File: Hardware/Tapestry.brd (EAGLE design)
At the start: 76.2 x 73.7 mm, 106 parts, among them J1 CORTEX_DEBUGPTH, J2 POWER_JACKPTH_LOCK, U1 ATSAMS70NXXA-AN, U2 AK4618VQSFE-PACKAGE, U3 LM1117, U4 LM1117, Y1 12MHz

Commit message: Routing in progress.
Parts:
- added J10: 3.3V, SparkFun-Passives:TP_15TH
- added J11: VIN, SparkFun-Passives:TP_15TH
- added J3: AOUT4L, SparkFun-Passives:TP_15TH
- added J4: AOUT4R, SparkFun-Passives:TP_15TH
- added J5: AOUT5L, SparkFun-Passives:TP_15TH
- added J6: AOUT5R, SparkFun-Passives:TP_15TH
- added J7: AIN3R, SparkFun-Passives:TP_15TH
- added J8: AIN3L, SparkFun-Passives:TP_15TH
- added J9: 3.3VA, SparkFun-Passives:TP_15TH
- TP2: device SparkFun-Connectors:1X06_NO_SILK -> SparkFun-Connectors:1X07_NO_SILK
- moved SJ2 6.60 mm to (54.9, 45.4)
- moved C34 5.08 mm to (44.5, 26.7)
- moved C3 4.58 mm to (36.8, 35.6)
- moved C4 4.58 mm to (36.8, 34.3)
- moved L1 4.58 mm to (33.0, 35.6)
- moved L2 4.58 mm to (33.0, 34.3)
- moved R23 3.05 mm to (18.5, 8.89)
- moved C12 2.79 mm to (23.1, 54.6), turned to 180 degrees
- moved C33 2.79 mm to (23.1, 55.9)
- moved R25 2.79 mm to (23.9, 45.7)
- moved R26 2.79 mm to (23.9, 47.0)
- moved R3 2.79 mm to (23.1, 50.8)
- moved R4 2.79 mm to (23.1, 53.3)
- moved C14 2.65 mm to (36.3, 62.2), turned to 90 degrees
- moved R14 2.54 mm to (44.5, 25.4)
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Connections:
- new net N$28: J7.P$1, U2.23
- new net N$30: J8.P$1, U2.21
- new net N$31: J3.P$1, U2.30
- new net N$32: J4.P$1, U2.29
- new net N$33: J5.P$1, U2.28
- new net N$34: J6.P$1, U2.27
- net 3.3V: now also J10.P$1
- net 3.3V_A: now also J9.P$1
- net APDN: now also TP2.7
- net VIN: now also J11.P$1
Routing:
- net 3.3V: track 0.00 -> 227.2 mm, vias 0 -> 12
- net 3.3V_A: track 0.00 -> 77.3 mm, vias 0 -> 2
- net TDMI: track 0.00 -> 63.2 mm, vias 0 -> 2
- net VDDOUT: track 0.00 -> 62.9 mm
- net SDCD: track 0.00 -> 60.8 mm, vias 0 -> 4
- net SDD3: track 0.00 -> 59.2 mm, vias 0 -> 2
- net NRESET: track 0.00 -> 57.3 mm, vias 0 -> 2
- net SDCLK: track 0.00 -> 53.0 mm, vias 0 -> 3
- net SDD2: track 0.00 -> 50.5 mm, vias 0 -> 2
- net N$7: track 0.00 -> 48.4 mm
- net SDCMD: track 0.00 -> 47.0 mm, vias 0 -> 1
- net N$9: track 0.00 -> 39.9 mm, vias 0 -> 2
- net VIN: track 0.00 -> 39.1 mm
- net SDD0: track 0.00 -> 34.2 mm, vias 0 -> 3
- net UIA1: track 0.00 -> 33.0 mm
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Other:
- board text added: "APDN"

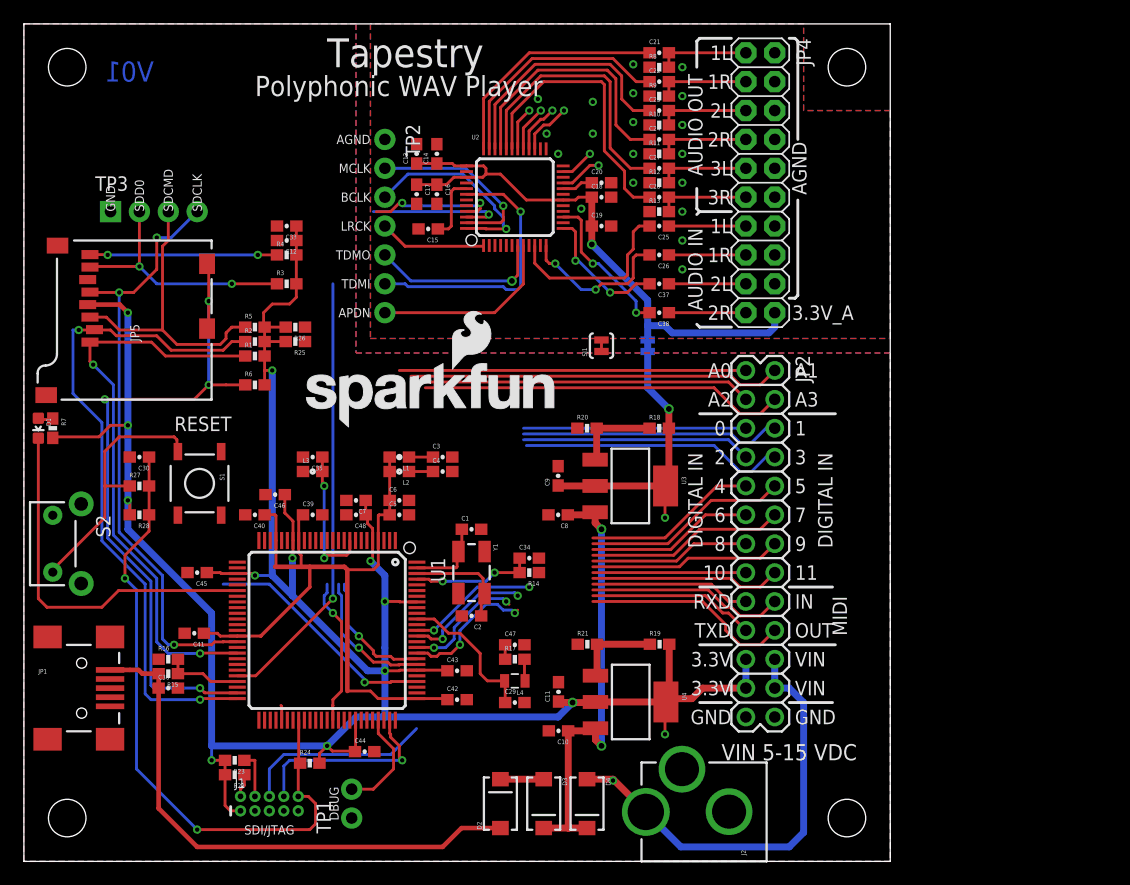
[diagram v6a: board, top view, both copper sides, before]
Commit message: Routing nearly complete.
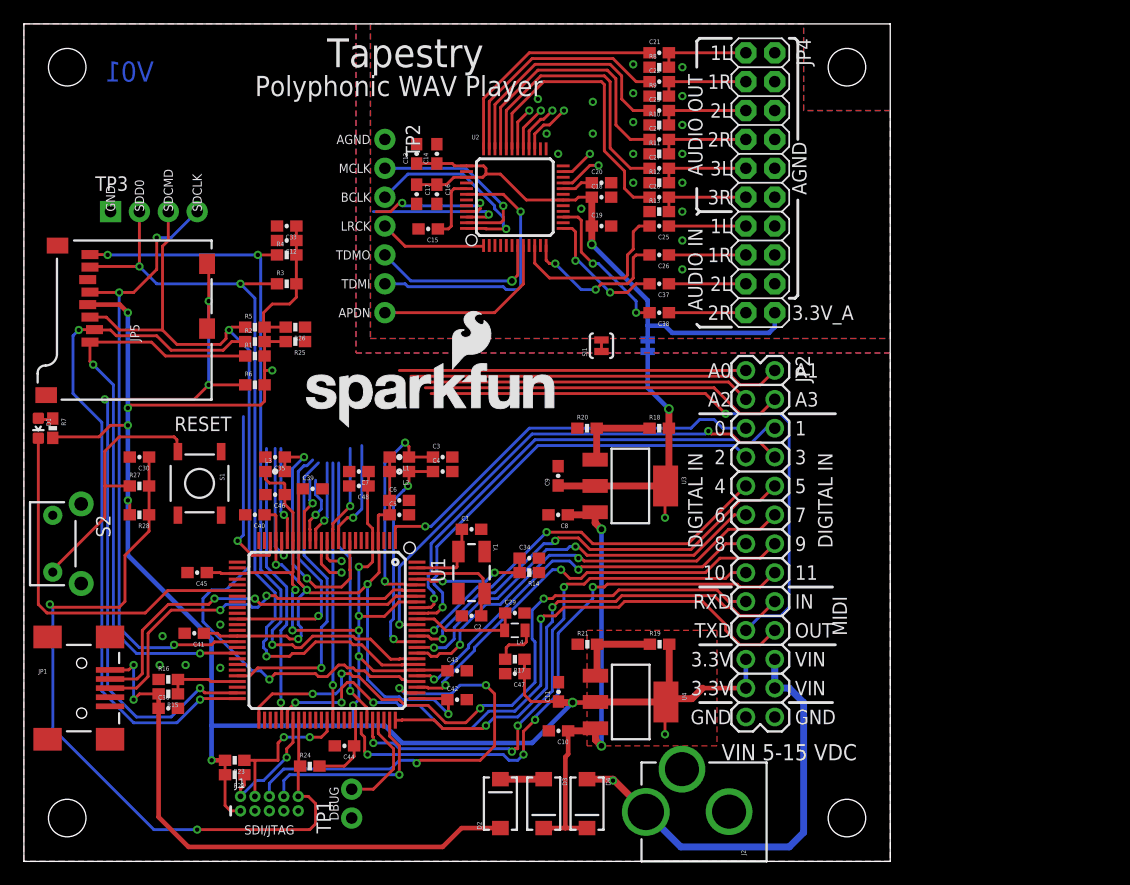
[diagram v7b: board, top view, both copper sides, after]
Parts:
- added J12: A4, SparkFun-Passives:TP_15TH
- added J13: A5, SparkFun-Passives:TP_15TH
- moved C29 7.87 mm to (43.2, 21.8)
- moved L4 4.45 mm to (43.2, 20.3)
- moved C35 3.30 mm to (22.1, 35.6)
- moved L3 3.30 mm to (22.1, 34.3)
- moved C48 2.55 mm to (29.5, 33.0)
- moved C7 2.55 mm to (29.5, 34.3)
- moved C47 2.54 mm to (43.2, 16.5), turned to 180 degrees
- moved C39 2.29 mm to (25.4, 32.8)
- moved C44 1.85 mm to (28.2, 10.2), turned to 180 degrees
- moved R15 1.78 mm to (12.7, 14.7)
- moved R16 1.78 mm to (12.7, 16.0)
- moved C36 1.78 mm to (12.7, 13.5)
- moved R24 0.25 mm to (25.1, 8.38)
- turned R17 to 180 degrees
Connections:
- new net N$35: J12.P$1, U1.14
- new net N$36: J13.P$1, U1.13
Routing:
- net TXD: track 14.7 -> 69.4 mm, vias 0 -> 2
- net RXD: track 14.1 -> 57.1 mm, vias 0 -> 4
- net MOUT: track 18.4 -> 57.6 mm, vias 0 -> 4
- net SDD1: track 27.7 -> 66.0 mm
- net SDD0: track 34.2 -> 71.1 mm
- net UID11: track 16.8 -> 51.4 mm, vias 0 -> 4
- net UID10: track 13.5 -> 47.6 mm, vias 0 -> 4
- net HSDP: track 0.00 -> 33.4 mm, vias 0 -> 2
- net HSDM: track 0.00 -> 32.7 mm, vias 0 -> 2
- net SDCMD: track 47.0 -> 77.3 mm, vias 1 -> 2
- net MIN: track 17.5 -> 43.7 mm, vias 0 -> 2
- net APDN: track 16.6 -> 40.3 mm, vias 0 -> 1
- net I2C_SCK: track 13.6 -> 37.2 mm, vias 1 -> 2
- net TDMO: track 15.4 -> 38.2 mm, vias 1 -> 2
- net UID3: track 23.3 -> 45.7 mm, vias 0 -> 2
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- added copper zone on layer 1, net 3.3V

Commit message: Routing nearly complete.
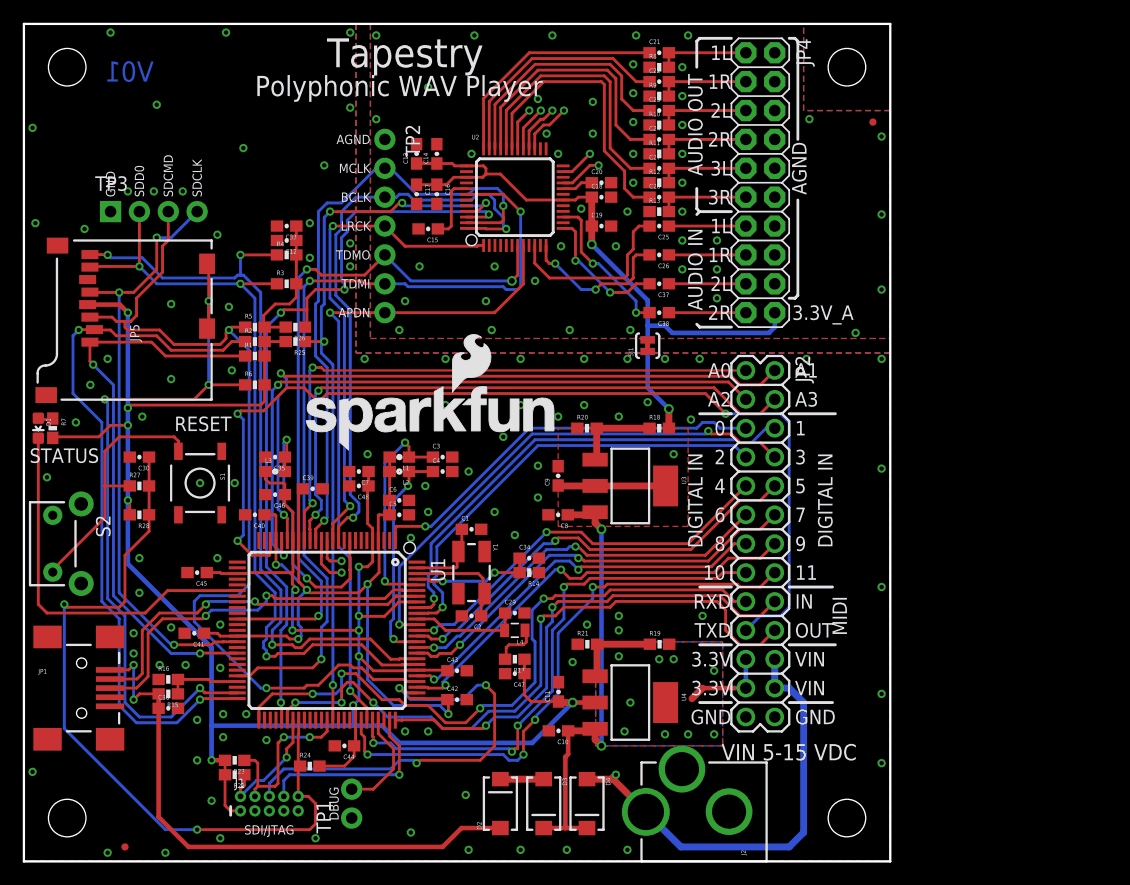
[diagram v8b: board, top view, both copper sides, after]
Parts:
- added FD1, FD2: FIDUCIALUFIDUCIAL, SparkFun-Aesthetics:MICRO-FIDUCIAL
- moved FRAME1 7.62 mm to (-1.27, -27.9)
- moved J10 6.65 mm to (57.1, 17.8)
- moved J9 5.64 mm to (57.1, 35.8)
- moved SJ1 4.06 mm to (54.9, 45.4)
- moved LOGO1 2.03 mm to (24.1, 36.1)
- moved J11 0.57 mm to (52.1, 7.62)
- moved U4 0.06 mm to (53.3, 14.0)
- moved S1 0.05 mm to (15.5, 33.3)
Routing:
- net MCLK: track 23.6 -> 54.7 mm
- net I2C_SCK: track 37.2 -> 67.4 mm, vias 2 -> 4
- net I2C_SDA: track 34.3 -> 63.8 mm, vias 3 -> 5
- net BCLK: track 27.1 -> 52.2 mm
- net LRCK: track 18.1 -> 43.2 mm, vias 1 -> 2
- net TDMO: track 38.2 -> 62.4 mm, vias 2 -> 3
- net TDMI: track 51.5 -> 73.5 mm, vias 2 -> 3
- net TXD: track 69.4 -> 88.3 mm, vias 2 -> 3
- net UIA1: track 41.3 -> 60.1 mm, vias 1 -> 2
- net APDN: track 40.3 -> 58.6 mm, vias 1 -> 2
- net UIA2: track 40.7 -> 58.9 mm, vias 1 -> 2
- net UIA0: track 36.2 -> 53.9 mm, vias 1 -> 2
- net UIA3: track 38.3 -> 55.8 mm, vias 1 -> 2
- net 3.3V: track 239.7 -> 222.9 mm, vias 14 -> 21
- net 3.3V_A: track 77.3 -> 69.8 mm
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- added copper zone on layer 16, net 3.3V
- added copper zone on layer 1, net 3.3V_A
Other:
- board text added: "4x 0.130" holes, to clear 4-40 screws."
- board text added: "All dimensions in inches."
- board text added: "STATUS"
